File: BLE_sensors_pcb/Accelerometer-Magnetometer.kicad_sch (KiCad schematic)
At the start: 6 parts, among them U3 TPS63031DSK

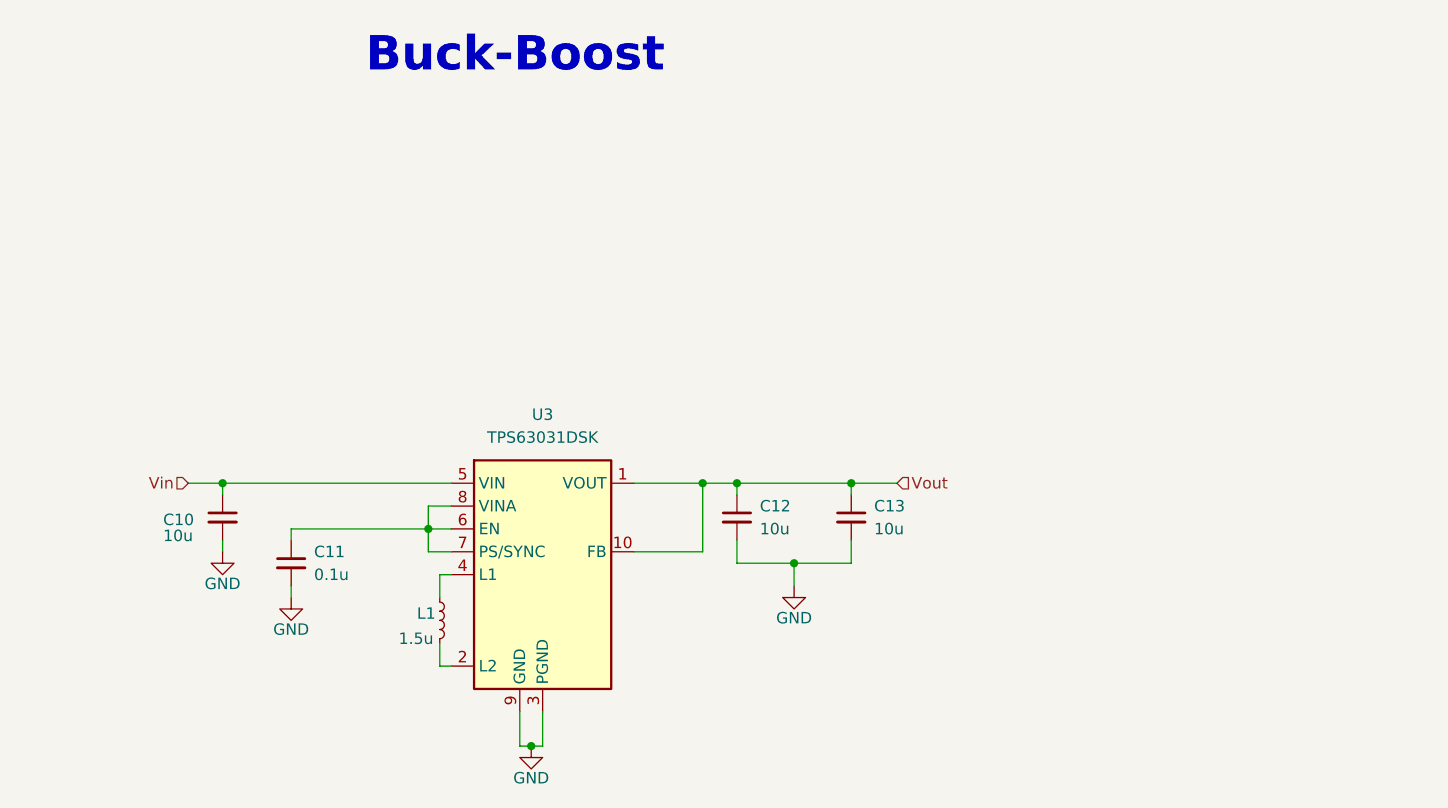
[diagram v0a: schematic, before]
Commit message: Added the usb to serial bridge
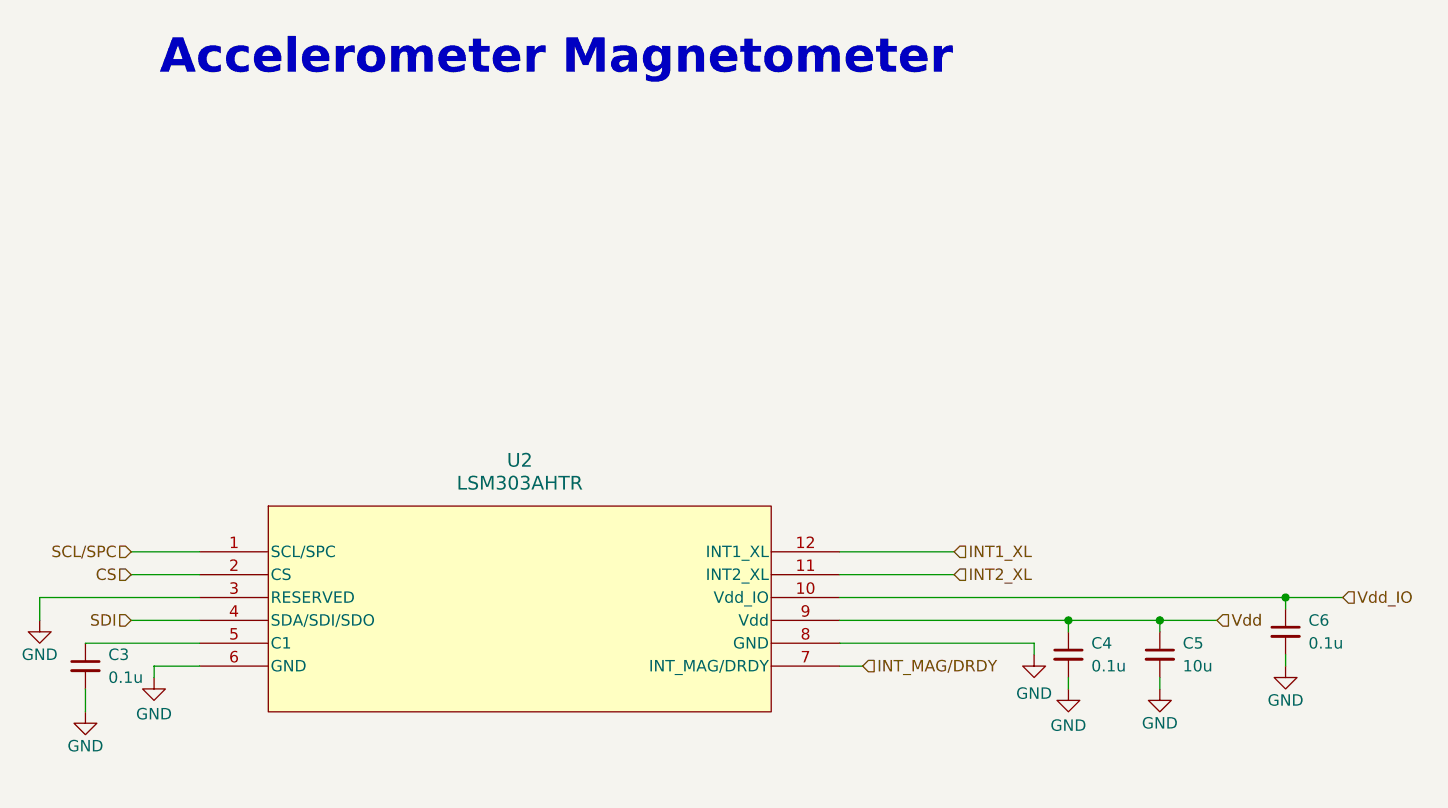
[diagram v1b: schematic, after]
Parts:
- removed C10, C12, C13: 10u, symbol Device:C_Small
- removed C11: 0.1u, symbol Device:C_Small
- removed L1: 1.5u, symbol Device:L_Small
- removed U3: TPS63031DSK, Package_SON:WSON-10-1EP_2.5x2.5mm_P0.5mm_EP1.2x2mm, symbol Regulator_Switching:TPS63031DSK
- added C3, C4, C6: 0.1u, symbol Device:C_Small
- added C5: 10u, symbol Device:C_Small
- added U2: LSM303AHTR, My_Libraries:LSM303AHTR, symbol My_Libraries:LSM303AHTR
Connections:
- net GND: now also C3.2, C4.2, C5.2, C6.2, U2.3 (RESERVED), U2.6 (GND), U2.8 (GND)
- new net: C3.1, U2.5 (C1)
- new net CS: U2.2 (CS)
- new net INT1_XL: U2.12 (INT1_XL)
- new net INT2_XL: U2.11 (INT2_XL)
- new net INT_MAG/DRDY: U2.7 (INT_MAG/DRDY)
- new net SCL/SPC: U2.1 (SCL/SPC)
- new net SDI: U2.4 (SDA/SDI/SDO)
- new net Vdd: C4.1, C5.1, U2.9 (Vdd)
- new net Vdd_IO: C6.1, U2.10 (Vdd_IO)
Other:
- note added: "Accelerometer Magnetometer"
- note removed: "Buck-Boost"

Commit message: Footprints and some pcb placement
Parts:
- C3, C4, C6: footprint (none) -> Capacitor_SMD:C_0603_1608Metric
- C5: footprint (none) -> Capacitor_SMD:C_0805_2012Metric
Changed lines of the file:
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@@
 			)
 		)
-		(property "Footprint" ""
+		(property "Footprint" "Capacitor_SMD:C_0805_2012Metric"
 			(at 212.09 109.22 0)
 			(effects
@@
 			)
 		)
-		(property "Footprint" ""
+		(property "Footprint" "Capacitor_SMD:C_0603_1608Metric"
 			(at 92.71 110.49 0)
 			(effects
@@
 			)
 		)
-		(property "Footprint" ""
+		(property "Footprint" "Capacitor_SMD:C_0603_1608Metric"
 			(at 226.06 106.68 0)
 			(effects
@@
 			)
 		)
-		(property "Footprint" ""
+		(property "Footprint" "Capacitor_SMD:C_0603_1608Metric"
 			(at 201.93 109.22 0)
 			(effects
